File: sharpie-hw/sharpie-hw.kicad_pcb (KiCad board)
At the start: 2 copper layers, 76 parts, among them J1 Conn_01x03_MountingPin, J4 Conn_01x11, J6 Conn_01x02_MountingPin, J8 LS021B7DD02, SW1 SW_Push_Cross, SW2 SW_Push_Cross, SW3 SW_Push_Cross, U1 TPS7A2533, U2 TPS7A2501, U3 RP2350_60QFN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

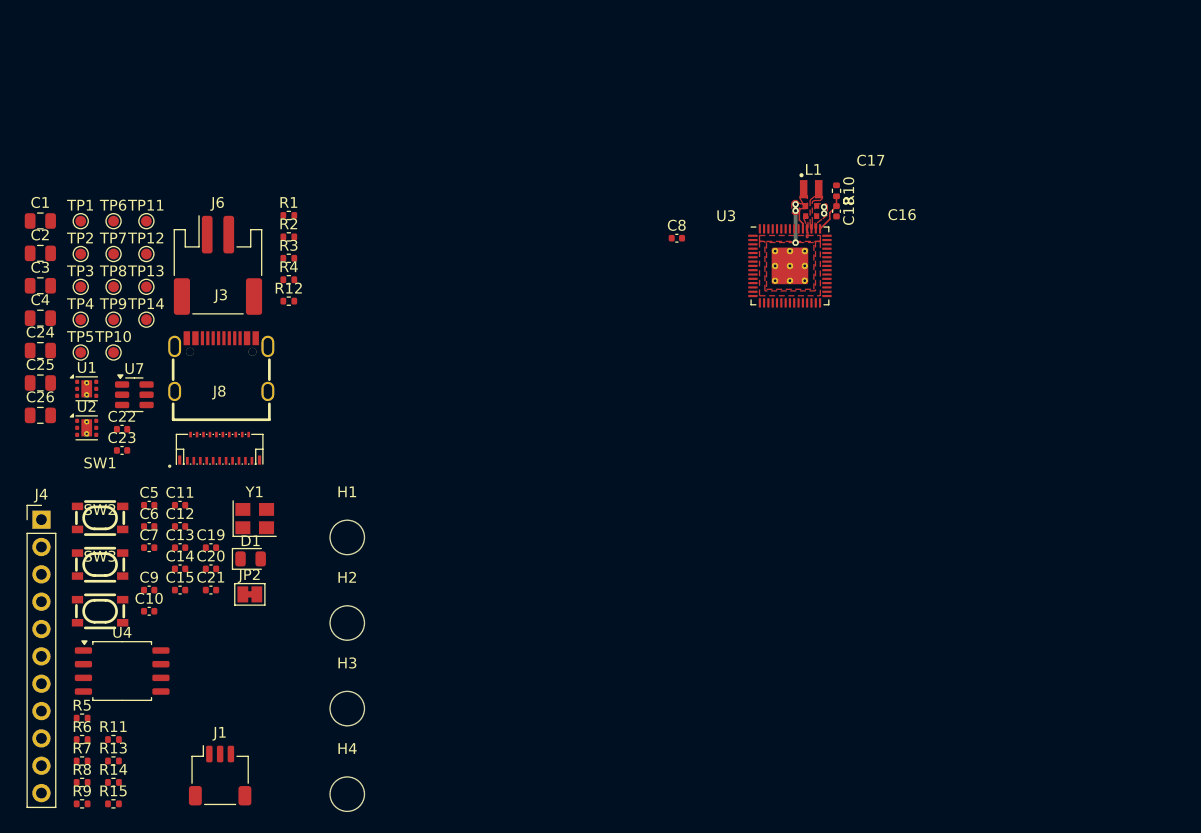
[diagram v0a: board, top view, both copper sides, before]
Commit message: Modify FPC footprint, add alternate USB-C footprint, and commit final (before review) design.
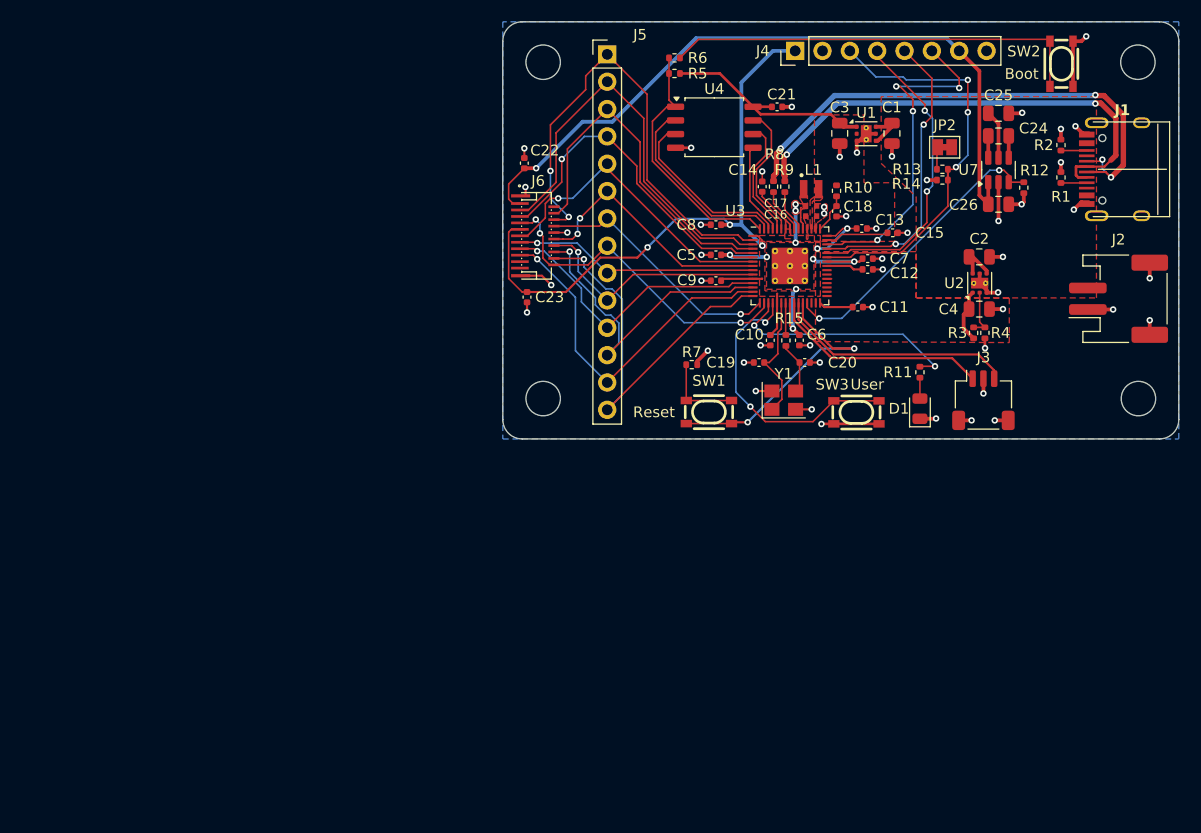
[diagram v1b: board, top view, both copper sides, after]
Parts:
- removed TP1, TP10, TP11, TP12, TP13, TP14, TP2, TP3, TP4, TP5, TP6, TP7, TP8, TP9: TestPoint, TestPoint:TestPoint_Pad_D1.0mm
- added J5: Conn_01x14, Connector_PinHeader_2.54mm:PinHeader_1x14_P2.54mm_Vertical, F.Cu at (202.6, 68.2)
- J1: renamed from J3; footprint Sharpie:USB-C_SMD-TYPE-C-31-M-12 -> Sharpie:TYPE-C-31-M-12
- J4: value Conn_01x11 -> Conn_01x08; footprint Connector_PinHeader_2.54mm:PinHeader_1x11_P2.54mm_Vertical -> Connector_PinHeader_2.54mm:PinHeader_1x08_P2.54mm_Vertical
- moved SW2 100.7 mm to (244.8, 69.0), turned to -90 degrees
- moved R14 95.2 mm to (233.7, 79.8), turned to 180 degrees
- moved R13 94.6 mm to (233.7, 78.8)
- moved C25 92.5 mm to (238.9, 73.7)
- moved C24 91.2 mm to (238.9, 75.8), turned to 180 degrees
- moved C26 91.1 mm to (238.9, 82.1)
- moved H2 90.1 mm to (251.9, 68.9)
- moved J1 87.4 mm to (252.2, 78.8), turned to 90 degrees
- moved C4 87.2 mm to (237.2, 91.8)
- moved C2 87.2 mm to (237.2, 87.0)
- moved R9 86.9 mm to (219.1, 80.5), turned to 90 degrees
- moved R8 84.8 mm to (218.1, 80.5), turned to 90 degrees
- moved U2 84.0 mm to (237.2, 89.4), turned to 90 degrees
- moved R6 83.9 mm to (208.8, 68.5), turned to 180 degrees
- moved J2 83.7 mm to (250.1, 90.9), turned to 90 degrees
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- renumbered J6 to J2, J1 to J3, J8 to J6
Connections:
- J4 pad 3: /MCU/EX_B1 -> /MCU/EX_B4
- J4 pad 4: /MCU/EX_B2 -> /MCU/EX_B5
- J4 pad 5: /MCU/EX_B3 -> /MCU/EX_B6
- J4 pad 6: /MCU/EX_B4 -> /MCU/EX_B7
- J4 pad 7: /MCU/EX_B5 -> +5V
- J4 pad 8: /MCU/EX_B6 -> GND
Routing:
- net +3.2V: track 0.00 -> 81.8 mm, vias 0 -> 5
- net GND: track 0.00 -> 73.1 mm, vias 2 -> 50
- net +5V: track 0.00 -> 68.5 mm, vias 0 -> 1
- net D+: track 0.00 -> 49.8 mm, vias 0 -> 4
- net D-: track 0.00 -> 46.7 mm, vias 0 -> 2
- net INTB: track 0.00 -> 44.8 mm, vias 0 -> 2
- net Net-(SW2-2): track 0.00 -> 39.4 mm
- net GSP: track 0.00 -> 38.5 mm
- net /MCU/EX_B4: track 0.00 -> 38.1 mm, vias 0 -> 3
- net B1: track 0.00 -> 37.4 mm, vias 0 -> 1
- net GCK: track 0.00 -> 33.3 mm
- net B0: track 0.00 -> 32.5 mm, vias 0 -> 1
- net /MCU/EX_B7: track 0.00 -> 31.8 mm, vias 0 -> 4
- net +3.3V: track 0.00 -> 31.4 mm
- net GEN: track 0.00 -> 31.0 mm, vias 0 -> 1
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- added copper zone on B.Cu, net GND
- added copper zone on F.Cu, net VCC
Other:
- board outline added: 62.8 x 38.8 mm
- board text added: "3.3V supply: via in filled zone 3.2V supply: filled area across board if possible 1V1: provided GND: filled zone on backside"
- board text added: "Boot"
- board text added: "Display is 35x46"
- board text added: "Idea: if the board has to be this tall anyway, make the test points a header or single-file spots"
- board text added: "Reset"
- board text added: "USB pair is 0.5mm wide at 0.2mm apart: https://electronics.stackexchange.com/a/495074"
- board text added: "User"

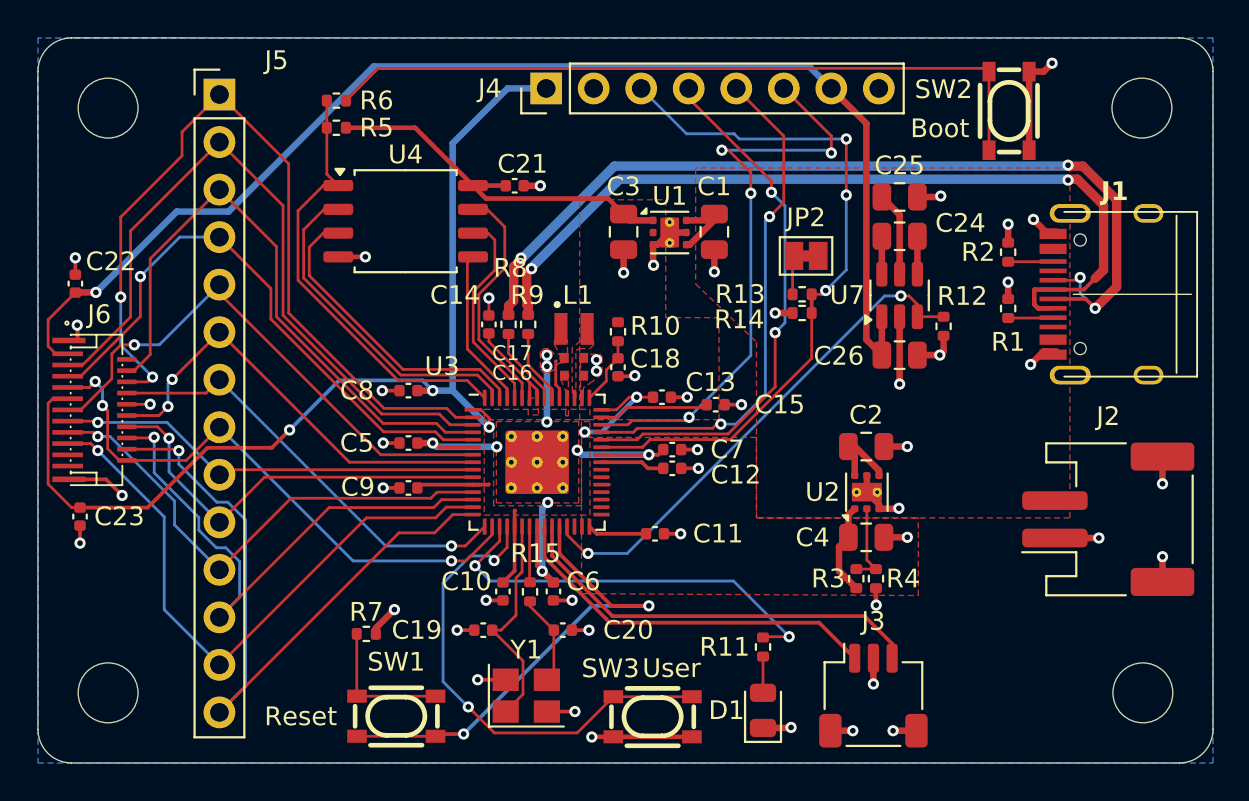
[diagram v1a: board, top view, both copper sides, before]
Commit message: Add all JLCPCB part numbers and some PCB silkscreens.
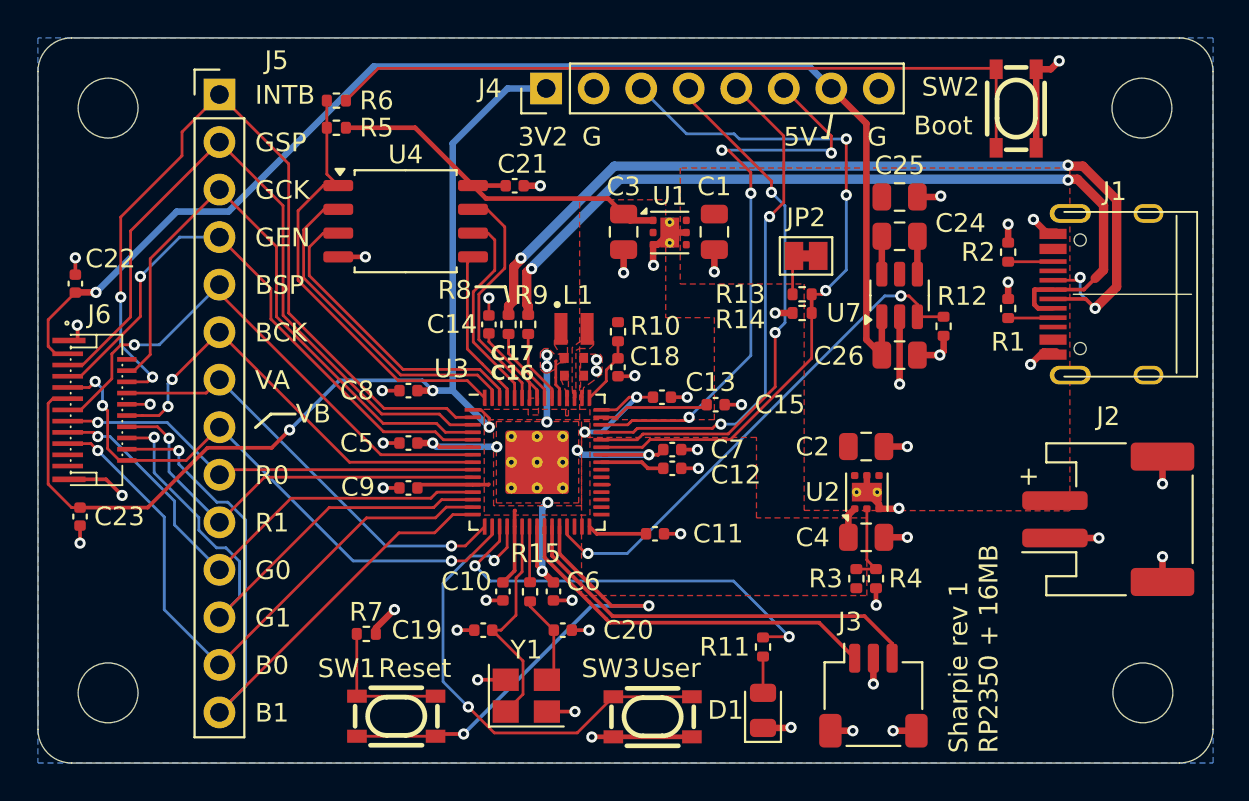
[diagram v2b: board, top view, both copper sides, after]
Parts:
- moved SW2 0.40 mm to (245.2, 68.9)
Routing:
- net VCC: track 12.7 -> 0.00 mm
- net +3.2V: track 81.8 -> 78.5 mm
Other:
- board text added: "+"
- board text added: "3V2"
- board text added: "5V"
- board text added: "B0"
- board text added: "B1"
- board text added: "BCK"
- board text added: "BSP"
- board text added: "G"
- board text added: "G0"
- board text added: "G1"
- board text added: "GCK"
- board text added: "GEN"
- board text added: "GSP"
- board text added: "INTB"
- board text added: "R0"
- board text added: "R1"
- board text added: "Sharpie rev 1 RP2350 + 16MB"
- board text added: "VA"
- board text added: "VB"

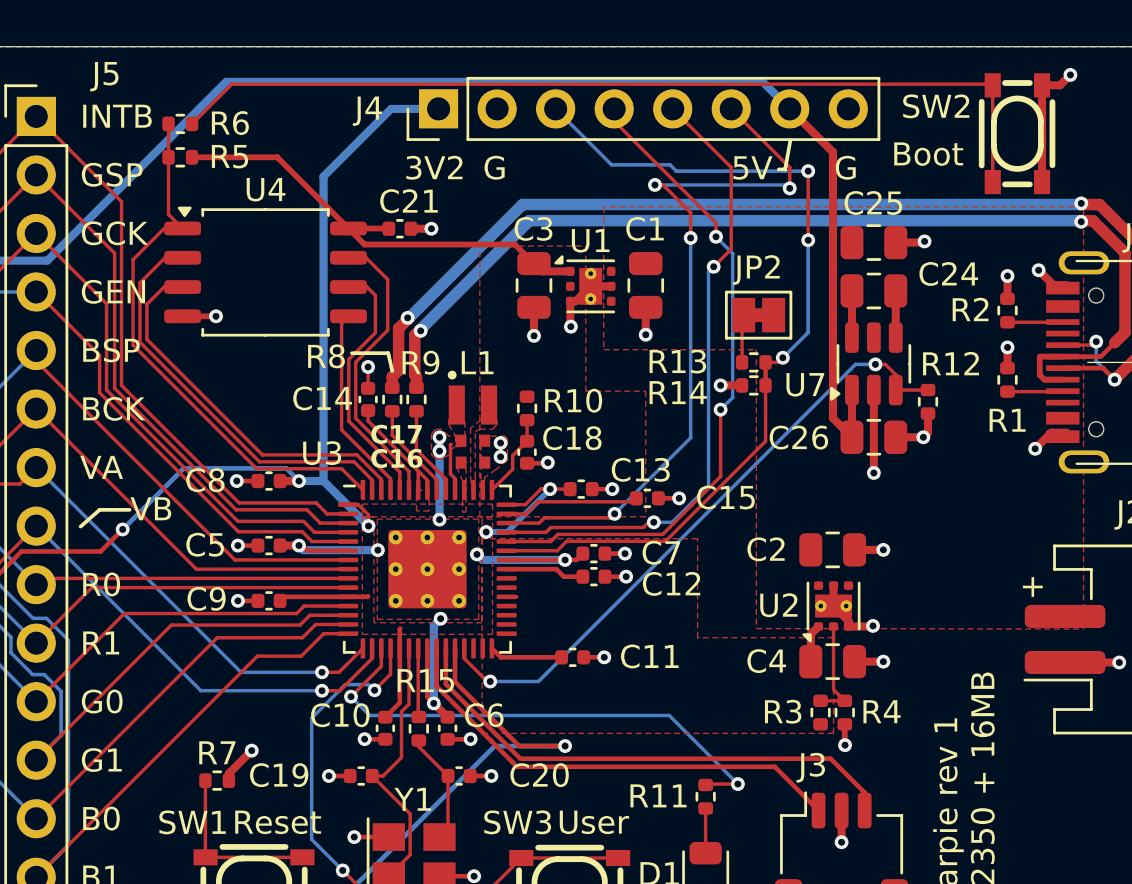
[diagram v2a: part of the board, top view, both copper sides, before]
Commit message: Fix some BOM entries and routing choices.
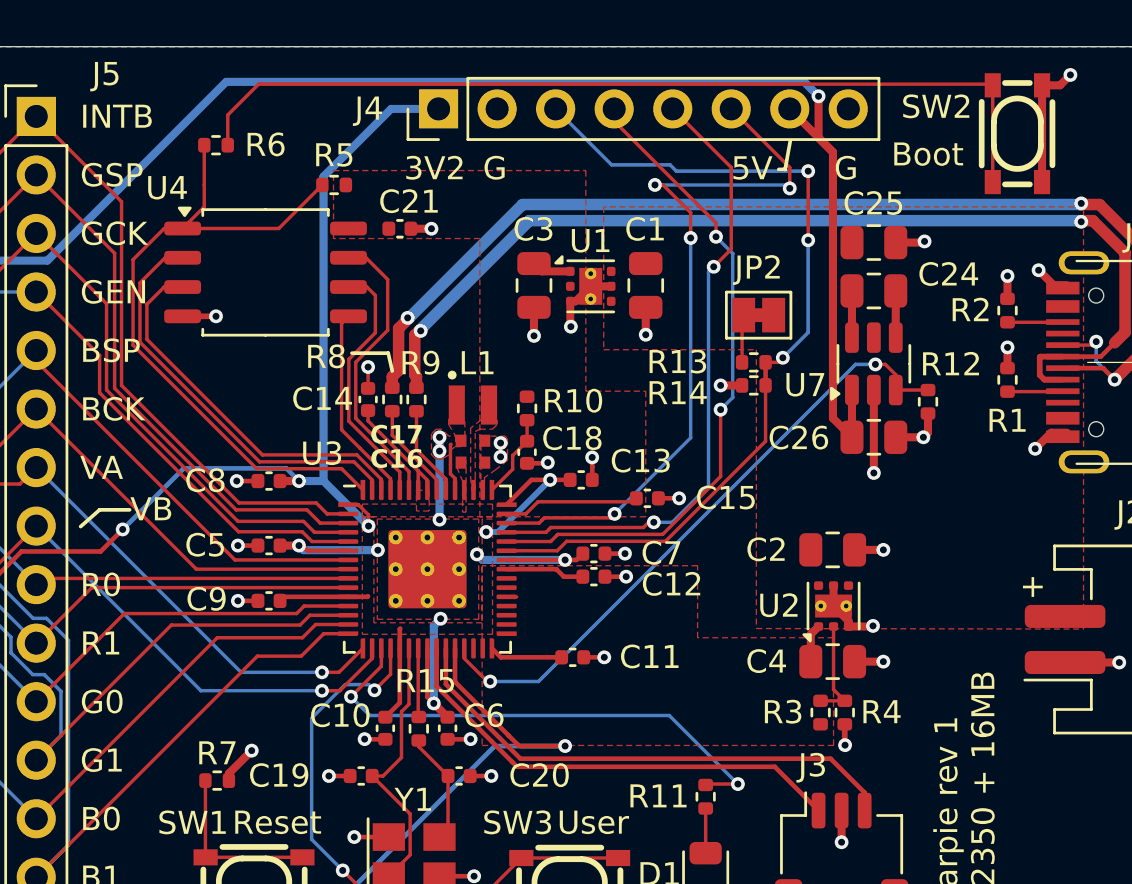
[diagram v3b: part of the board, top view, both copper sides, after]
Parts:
- moved R5 6.78 mm to (215.5, 71.2)
- moved R6 1.81 mm to (210.4, 69.4)
- moved C13 0.40 mm to (226.2, 84.0)
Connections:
- U3 pad 28: /MCU/EX_A2 -> unconnected-(U3-GPIO17-Pad28)
- U3 pad 29: /MCU/EX_A3 -> unconnected-(U3-GPIO18-Pad29)
- U3 pad 31: /MCU/EX_A4 -> unconnected-(U3-GPIO19-Pad31)
- U3 pad 32: /MCU/EX_A5 -> unconnected-(U3-GPIO20-Pad32)
- U3 pad 33: /MCU/EX_A6 -> unconnected-(U3-GPIO21-Pad33)
- U3 pad 34: /MCU/EX_A7 -> unconnected-(U3-GPIO22-Pad34)
- U3 pad 35: /MCU/EX_B1 -> unconnected-(U3-GPIO23-Pad35)
- U3 pad 36: /MCU/EX_B2 -> unconnected-(U3-GPIO24-Pad36)
- U3 pad 37: /MCU/EX_B3 -> unconnected-(U3-GPIO25-Pad37)
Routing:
- net +3.3V: track 31.4 -> 12.9 mm
- net /MCU/QSPI CS: track 23.8 -> 29.9 mm
- net +5V: track 68.5 -> 72.2 mm, vias 1 -> 2

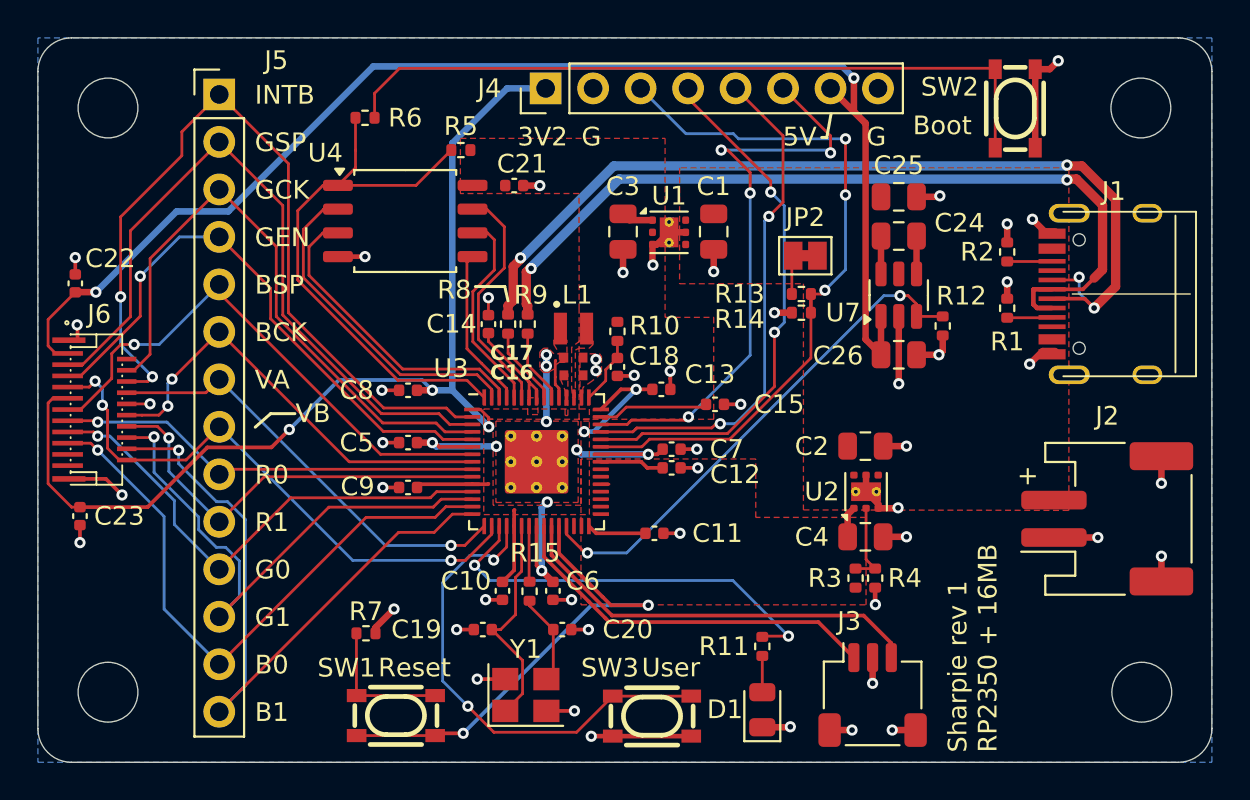
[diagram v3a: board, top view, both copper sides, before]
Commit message: Adjust display regulators to match datasheet, so they're now 1u 0805.
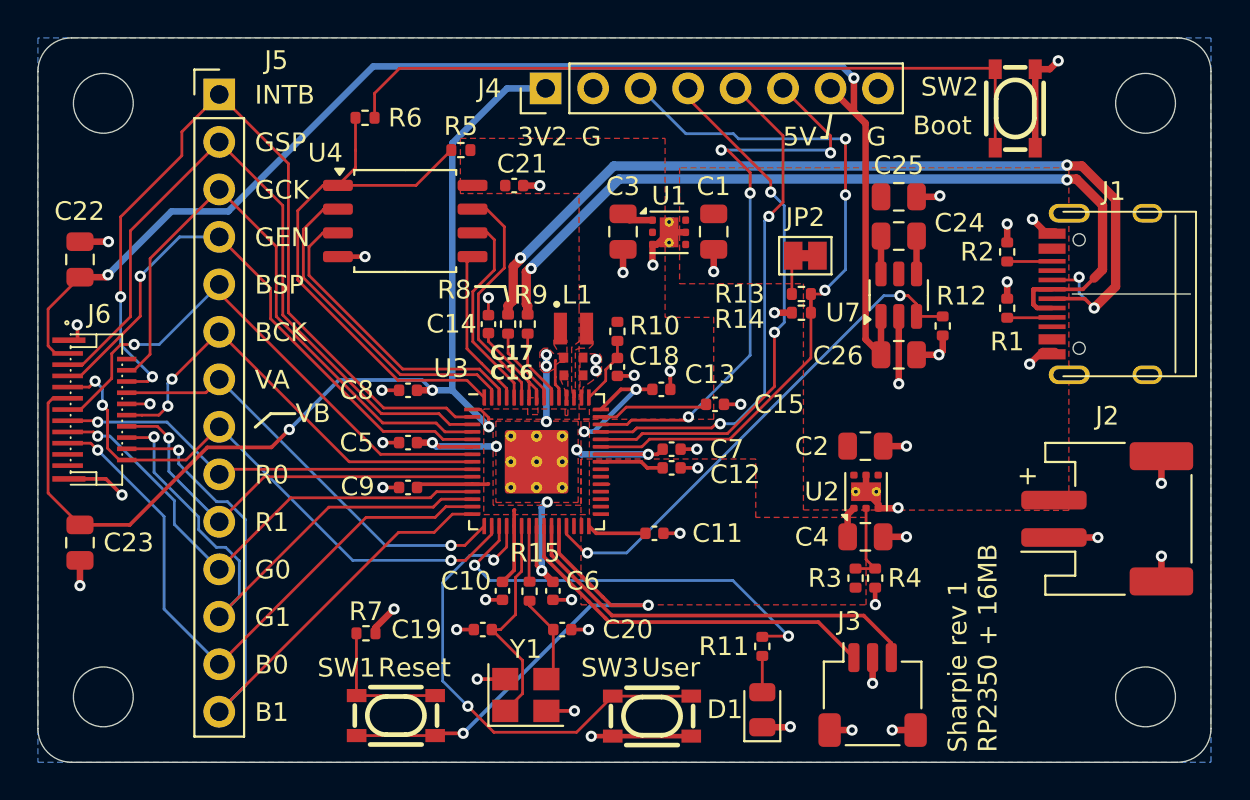
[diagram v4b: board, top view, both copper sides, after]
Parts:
- C22, C23: value 100n -> 1u; footprint Capacitor_SMD:C_0402_1005Metric -> Capacitor_SMD:C_0805_2012Metric
- moved C23 1.42 mm to (195.2, 92.2)
- moved C22 1.30 mm to (195.2, 77.0)
- moved H1 0.35 mm to (196.4, 68.7)
- moved H2 0.35 mm to (252.2, 68.7)
- moved H3 0.35 mm to (196.4, 100.4)
- moved H4 0.32 mm to (252.2, 100.4)
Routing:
- net +3.2V: track 78.8 -> 79.9 mm
- net GND: track 73.2 -> 74.3 mm
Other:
- board text removed: "3.3V supply: via in filled zone 3.2V supply: filled area across board if possible 1V1: provided GND: filled zone on backside"
- board text removed: "Idea: if the board has to be this tall anyway, make the test points a header or single-file spots"
